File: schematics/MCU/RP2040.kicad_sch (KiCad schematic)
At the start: 28 parts, among them J2 TC2030, SW1 SW_Push, U1 W25Q128JVS, U2 XC6206PxxxMR-Regulator_Linear, U3 RP2040, Y1 12MHz

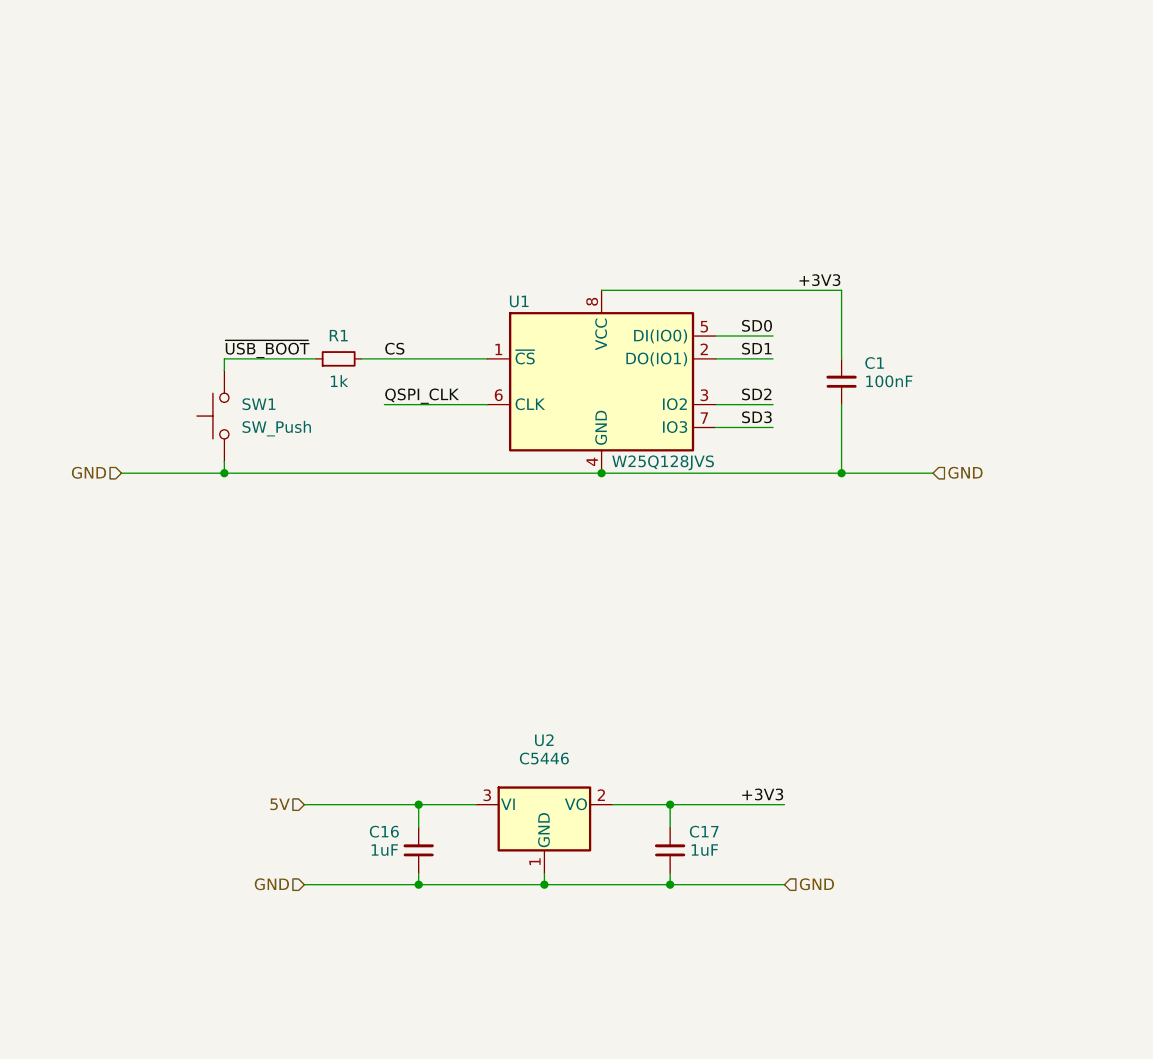
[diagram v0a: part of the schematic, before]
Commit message: restructure schematics folder
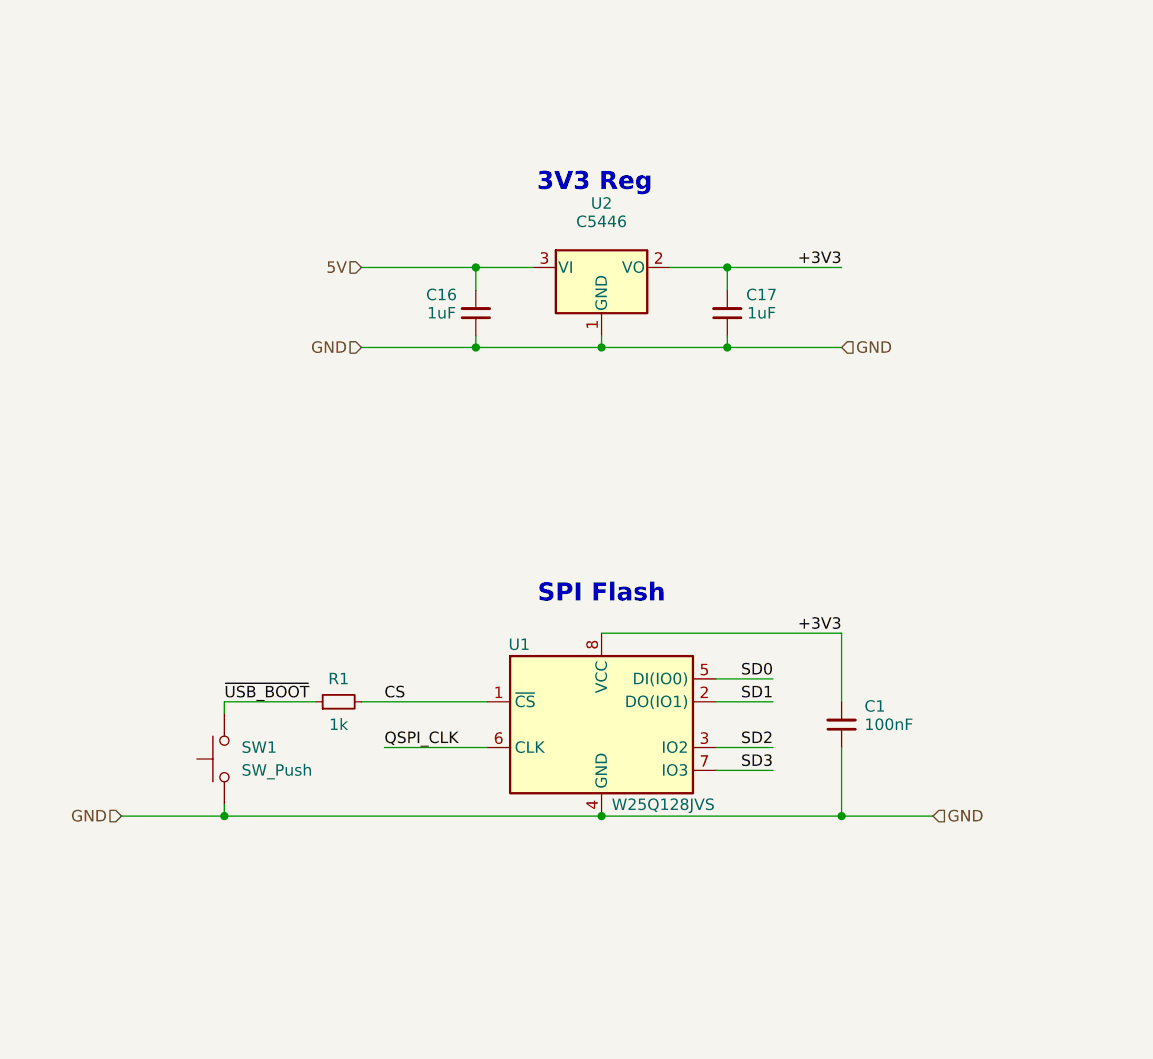
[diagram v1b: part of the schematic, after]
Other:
- note added: "3V3 Reg"
- note added: "SPI Flash"
- moved on the sheet: C1, C16, C17, R1, SW1, U1, U2

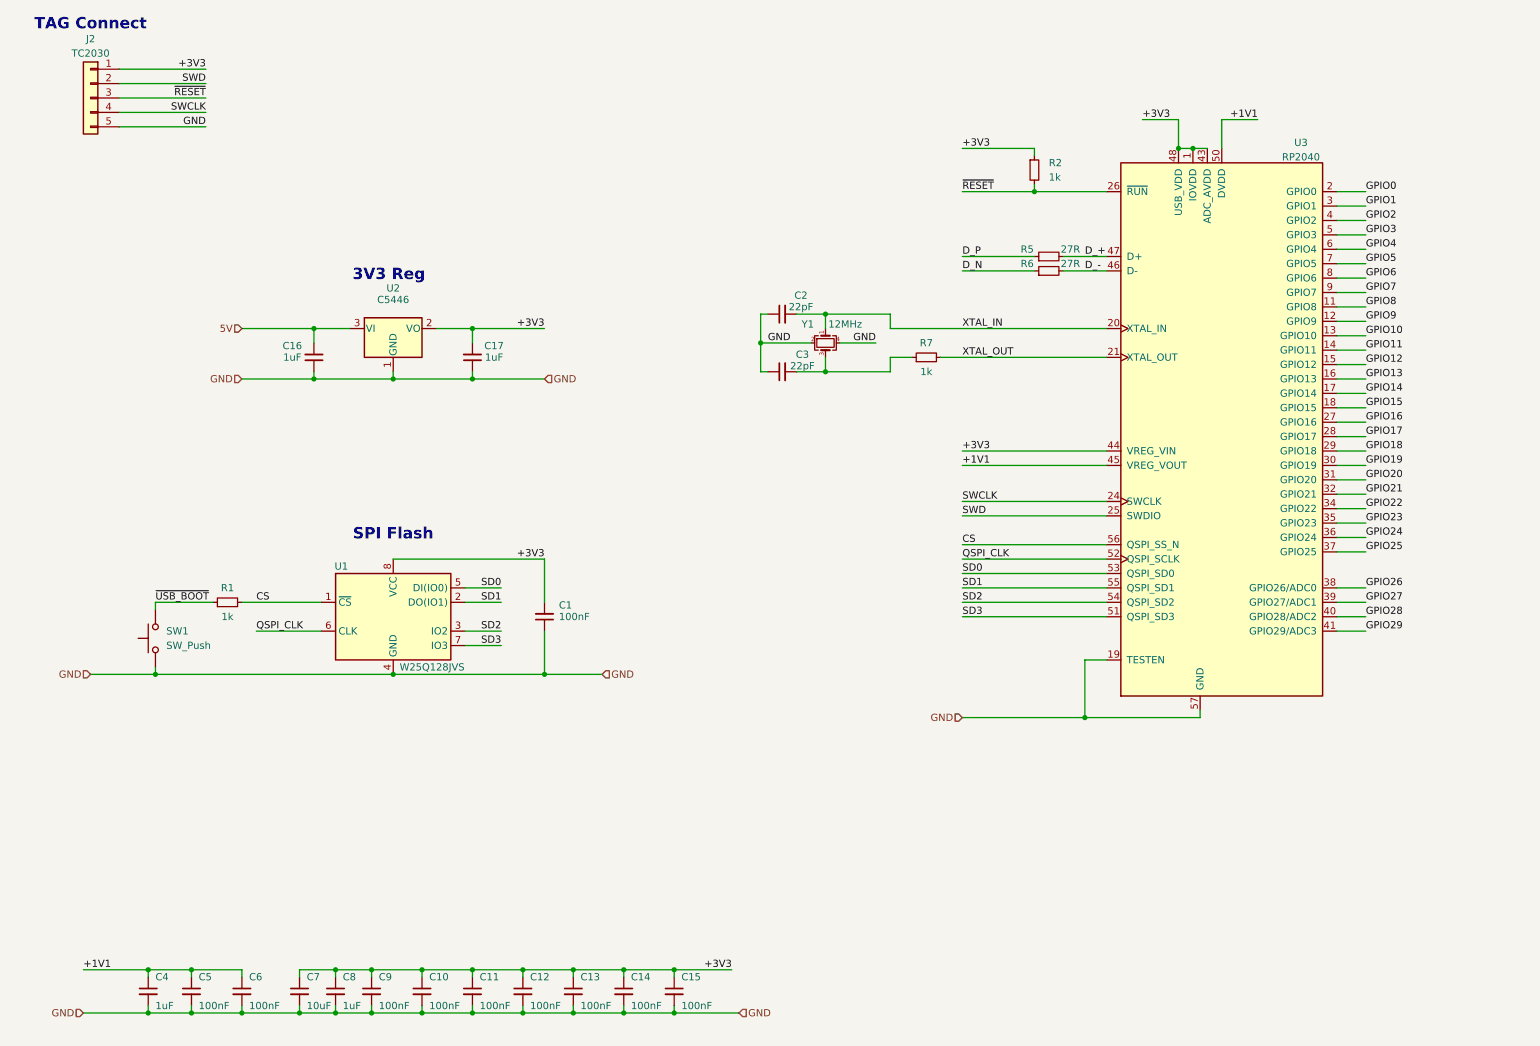
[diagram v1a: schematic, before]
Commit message: Add reset circuit to RP2040
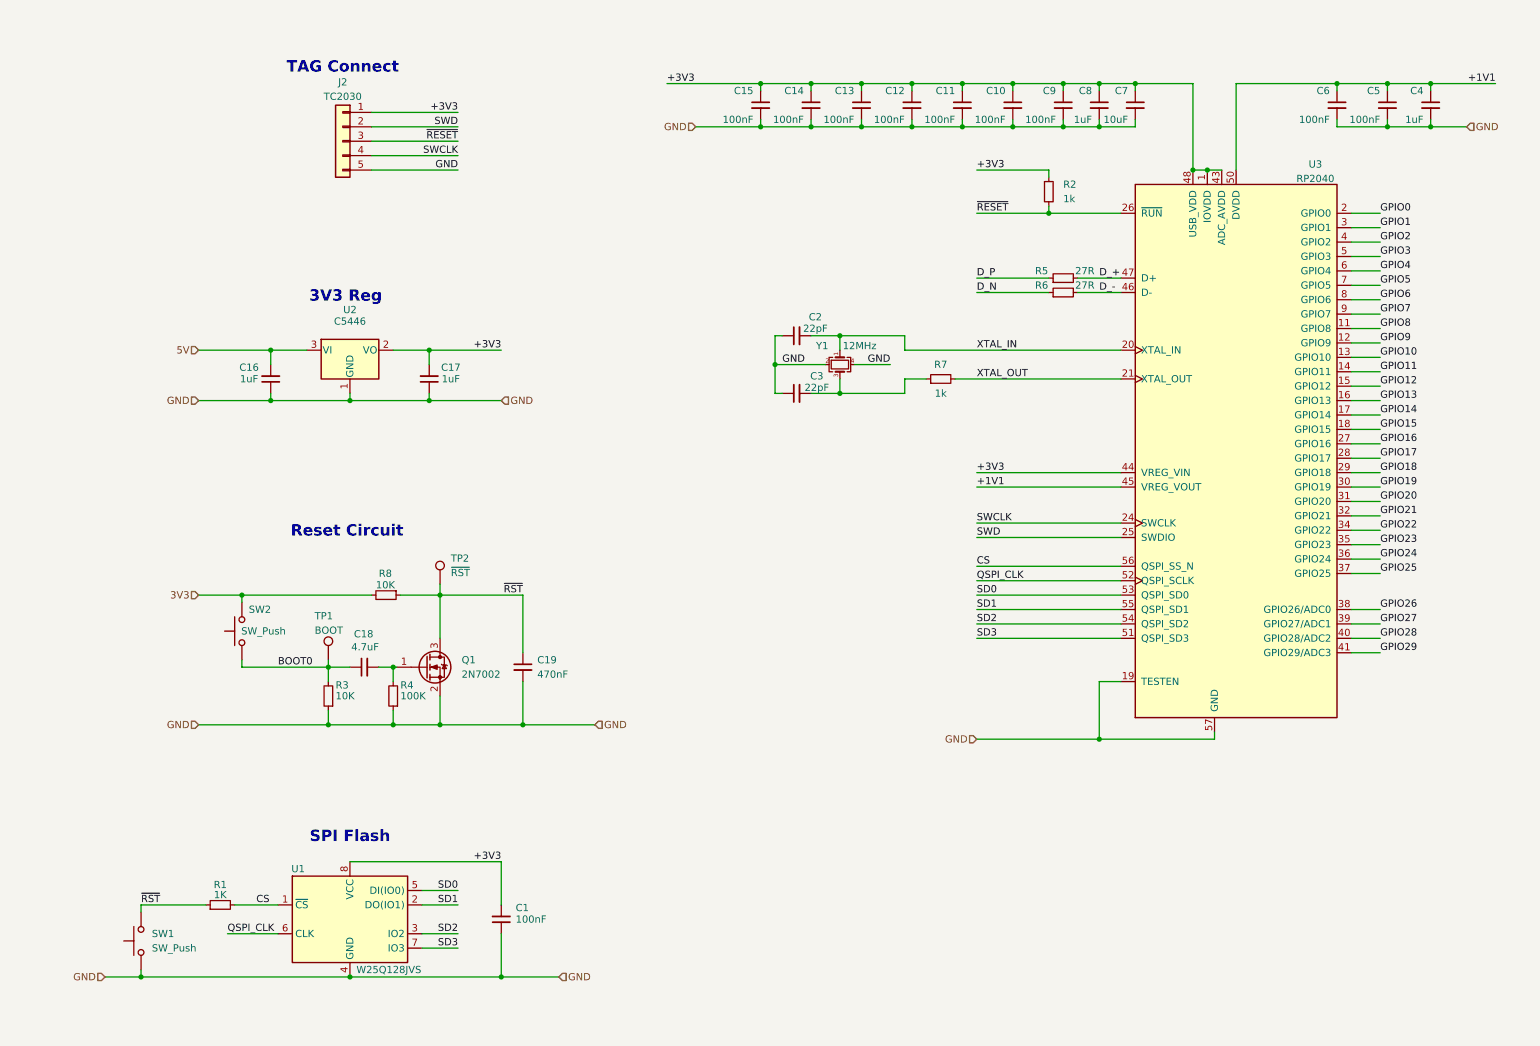
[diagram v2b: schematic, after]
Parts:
- added C18: 4.7uF, Capacitor_SMD:C_0603_1608Metric, symbol Device:C_Small
- added C19: 470nF, Capacitor_SMD:C_0603_1608Metric, symbol Device:C_Small
- added Q1: 2N7002, Package_TO_SOT_SMD:SOT-23, symbol Transistor_FET:2N7002
- added R3, R8: 10K, Resistor_SMD:R_0603_1608Metric, symbol Device:R_Small
- added R4: 100K, Resistor_SMD:R_0603_1608Metric, symbol Device:R_Small
- added SW2: SW_Push, symbol Switch:SW_Push
- added TP1: BOOT, symbol Connector:TestPoint
- added TP2: ~{RST}, symbol Connector:TestPoint
- R1: value 1k -> 1K
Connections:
- net GND: now also C19.2, Q1.2 (S), R3.1, R4.1
- net ~{USB_BOOT} renamed ~{RST}
- net ~{RST}: now also C19.1, Q1.3 (D), R8.1, TP2.1
- new net: C18.2, Q1.1 (G), R4.2
- new net 3V3: R8.2, SW2.1
- new net BOOT0: C18.1, R3.2, SW2.2, TP1.1
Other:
- note added: "Reset Circuit"
- moved on the sheet: C1, C10, C11, C12, C13, C14, C15, C16, C17, C2, C3, C4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

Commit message: Minor updates to STM32, refactor RP2040
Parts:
- removed C1: 100nF, Capacitor_SMD:C_0402_1005Metric, symbol Device:C_Small
- removed C16, C17: 1uF, Capacitor_SMD:C_0402_1005Metric, symbol Device:C_Small
- removed C18: 4.7uF, Capacitor_SMD:C_0603_1608Metric, symbol Device:C_Small
- removed C19: 470nF, Capacitor_SMD:C_0603_1608Metric, symbol Device:C_Small
- removed J2: TC2030, Connector:Tag-Connect_TC2030-IDC-NL_2x03_P1.27mm_Vertical, symbol Connector_Generic:Conn_01x05
- removed Q1: 2N7002, Package_TO_SOT_SMD:SOT-23, symbol Transistor_FET:2N7002
- removed R1: 1K, Resistor_SMD:R_0402_1005Metric, symbol Device:R_Small
- removed SW2: SW_Push, symbol Switch:SW_Push
- removed U1: W25Q128JVS, Package_SO:SOIC-8_5.23x5.23mm_P1.27mm, symbol Memory_Flash:W25Q128JVS
- added C11: 100nF, Capacitor_SMD:C_0402_1005Metric, symbol Device:C_Small
- added C6: 4.7uF, Capacitor_SMD:C_0805_2012Metric, symbol Device:C_Small
- added D20: LL4148, Diode_SMD:D_MiniMELF, symbol Diode:LL4148
- added J2: Conn_ARM_SWD_TagConnect_TC2030-NL, Connector:Tag-Connect_TC2030-IDC-NL_2x03_P1.27mm_Vertical, symbol Connector:Conn_ARM_SWD_TagConnect_TC2030-NL
- added Q1: 2N7002VC-7, Package_TO_SOT_SMD:SOT-363_SC-70-6, symbol Transistor_FET:FDG6335N
- added R5: 51K, Resistor_SMD:R_0402_1005Metric, symbol Device:R_Small
- added R6: 100K, Resistor_SMD:R_0402_1005Metric, symbol Device:R_Small
- added R7: 10K, Resistor_SMD:R_0402_1005Metric, symbol Device:R_Small
- added TP3: Boot, TestPoint:TestPoint_Pad_D1.0mm, symbol Connector:TestPoint
- added U3: GD25LQ128DYIGR, Package_SON:WSON-8-1EP_6x5mm_P1.27mm_EP3.4x4mm, symbol josh-memory:W25Q128JVSIQ
- C4, C8: value 1uF -> 10uF; LCSC C52923 -> (none); MPN (none) -> C0805C106K3PAC7800; Manufacturer (none) -> KEMET; Price (none) -> $0.43; Rating (none) -> CAP CER 10UF 25V X5R 0805; Supplier (none) -> Digikey; Supplier PN (none) -> 399-11939-1-ND
- C?: renamed from C12; LCSC C1525 -> (none); MPN (none) -> C0402C104K3RAC7867; Manufacturer (none) -> KEMET; Price (none) -> $0.33; Rating (none) -> CAP CER 0.1UF 25V X7R 0402; Supplier (none) -> Digikey; Supplier PN (none) -> 399-14148-1-ND
- C?: renamed from C7; LCSC C15525 -> (none); MPN (none) -> C0805C106K3PAC7800; Manufacturer (none) -> KEMET; Price (none) -> $0.43; Rating (none) -> CAP CER 10UF 25V X5R 0805; Supplier (none) -> Digikey; Supplier PN (none) -> 399-11939-1-ND
- C?: renamed from C15; LCSC C1525 -> (none); MPN (none) -> C0402C104K3RAC7867; Manufacturer (none) -> KEMET; Price (none) -> $0.33; Rating (none) -> CAP CER 0.1UF 25V X7R 0402; Supplier (none) -> Digikey; Supplier PN (none) -> 399-14148-1-ND
- C?: renamed from C14; LCSC C1525 -> (none); MPN (none) -> C0402C104K3RAC7867; Manufacturer (none) -> KEMET; Price (none) -> $0.33; Rating (none) -> CAP CER 0.1UF 25V X7R 0402; Supplier (none) -> Digikey; Supplier PN (none) -> 399-14148-1-ND
- C?: renamed from C11; LCSC C1525 -> (none); MPN (none) -> C0402C104K3RAC7867; Manufacturer (none) -> KEMET; Price (none) -> $0.33; Rating (none) -> CAP CER 0.1UF 25V X7R 0402; Supplier (none) -> Digikey; Supplier PN (none) -> 399-14148-1-ND
- C?: renamed from C10; LCSC C1525 -> (none); MPN (none) -> C0402C104K3RAC7867; Manufacturer (none) -> KEMET; Price (none) -> $0.33; Rating (none) -> CAP CER 0.1UF 25V X7R 0402; Supplier (none) -> Digikey; Supplier PN (none) -> 399-14148-1-ND
- C?: renamed from C2; LCSC C1555 -> (none); MPN (none) -> C0402C220J4GAC7867; Manufacturer (none) -> KEMET; Price (none) -> 0.16; Rating (none) -> CAP CER 22PF 16V C0G/NP0 0402; Supplier (none) -> Digikey; Supplier PN (none) -> 399-C0402C220J4GAC7867CT-ND
- C?: renamed from C13; LCSC C1525 -> (none); MPN (none) -> C0402C104K3RAC7867; Manufacturer (none) -> KEMET; Price (none) -> $0.33; Rating (none) -> CAP CER 0.1UF 25V X7R 0402; Supplier (none) -> Digikey; Supplier PN (none) -> 399-14148-1-ND
- C?: renamed from C5; LCSC C1525 -> (none); MPN (none) -> C0402C104K3RAC7867; Manufacturer (none) -> KEMET; Price (none) -> $0.33; Rating (none) -> CAP CER 0.1UF 25V X7R 0402; Supplier (none) -> Digikey; Supplier PN (none) -> 399-14148-1-ND
- C?: renamed from C3; LCSC C1555 -> (none); MPN (none) -> C0402C220J4GAC7867; Manufacturer (none) -> KEMET; Price (none) -> 0.16; Rating (none) -> CAP CER 22PF 16V C0G/NP0 0402; Supplier (none) -> Digikey; Supplier PN (none) -> 399-C0402C220J4GAC7867CT-ND
- C?: renamed from C9; LCSC C1525 -> (none); MPN (none) -> C0402C104K3RAC7867; Manufacturer (none) -> KEMET; Price (none) -> $0.33; Rating (none) -> CAP CER 0.1UF 25V X7R 0402; Supplier (none) -> Digikey; Supplier PN (none) -> 399-14148-1-ND
- C?: renamed from C6; LCSC C1525 -> (none); MPN (none) -> C0402C104K3RAC7867; Manufacturer (none) -> KEMET; Price (none) -> $0.33; Rating (none) -> CAP CER 0.1UF 25V X7R 0402; Supplier (none) -> Digikey; Supplier PN (none) -> 399-14148-1-ND
- R3: footprint Resistor_SMD:R_0603_1608Metric -> Resistor_SMD:R_0402_1005Metric; MPN (none) -> RC0402FR-0710KL; Manufacturer (none) -> YAGEO; Price (none) -> $0.16; Rating (none) -> RES 10K OHM 1% 1/16W 0402; Supplier (none) -> Digikey; Supplier PN (none) -> 311-10.0KLRCT-ND
- R4: value 100K -> 10K; footprint Resistor_SMD:R_0603_1608Metric -> Resistor_SMD:R_0402_1005Metric; MPN (none) -> RC0402FR-0710KL; Manufacturer (none) -> YAGEO; Price (none) -> $0.16; Rating (none) -> RES 10K OHM 1% 1/16W 0402; Supplier (none) -> Digikey; Supplier PN (none) -> 311-10.0KLRCT-ND
- R8: value 10K -> 1K; footprint Resistor_SMD:R_0603_1608Metric -> Resistor_SMD:R_0402_1005Metric; MPN (none) -> RC0402FR-071KL; Manufacturer (none) -> YAGEO; Price (none) -> $0.16; Rating (none) -> RES 1K OHM 1% 1/16W 0402; Supplier (none) -> Digikey; Supplier PN (none) -> 311-1.00KLRCT-ND
- R?: renamed from R2; value 1k -> 1K; LCSC C11702 -> (none); MPN (none) -> RC0402FR-071KL; Manufacturer (none) -> YAGEO; Price (none) -> $0.16; Rating (none) -> RES 1K OHM 1% 1/16W 0402; Supplier (none) -> Digikey; Supplier PN (none) -> 311-1.00KLRCT-ND
- R?: renamed from R5; footprint Resistor_SMD:R_0603_1608Metric -> Resistor_SMD:R_0402_1005Metric; LCSC C25190 -> (none); MPN (none) -> RC0402FR-0727RL; Manufacturer (none) -> YAGEO; Price (none) -> $0.16; Rating (none) -> RES 27 Ohms ±1% 0.063W, 1/16W Chip Resistor 0402 (1005 Metr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; Supplier (none) -> Digikey; Supplier PN (none) -> YAG3086CT-ND
- R?: renamed from R6; footprint Resistor_SMD:R_0603_1608Metric -> Resistor_SMD:R_0402_1005Metric; LCSC C25190 -> (none); MPN (none) -> RC0402FR-0727RL; Manufacturer (none) -> YAGEO; Price (none) -> $0.16; Rating (none) -> RES 27 Ohms ±1% 0.063W, 1/16W Chip Resistor 0402 (1005 Metr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; Supplier (none) -> Digikey; Supplier PN (none) -> YAG3086CT-ND
- R?: renamed from R7; value 1k -> 1K; LCSC C11702 -> (none); MPN (none) -> RC0402FR-071KL; Manufacturer (none) -> YAGEO; Price (none) -> $0.16; Rating (none) -> RES 1K OHM 1% 1/16W 0402; Supplier (none) -> Digikey; Supplier PN (none) -> 311-1.00KLRCT-ND
- SW1: value SW_Push -> SWITCH; footprint Connector_PinSocket_2.54mm:PinSocket_1x02_P2.54mm_Vertical -> (none); now in the parts list
- TP1: value BOOT -> Reset; footprint (none) -> TestPoint:TestPoint_Pad_D1.0mm
- TP2: value ~{RST} -> Delay; footprint (none) -> TestPoint:TestPoint_Pad_D1.0mm
- U?: renamed from U3; footprint Sleep-Lib:RP2040-QFN-56 -> Package_DFN_QFN:QFN-56-1EP_7x7mm_P0.4mm_EP3.2x3.2mm; LCSC C2040 -> (none); MPN (none) -> SC0914(13); Manufacturer (none) -> Raspberry Pi; Price (none) -> $1.11; Rating (none) -> IC MCU 32BIT EXT MEM 56QFN; Supplier (none) -> Digikey; Supplier PN (none) -> 2648-SC0914(13)CT-ND
- U?: renamed from U2; LCSC C5446 -> (none)
- Y?: renamed from Y1; footprint Crystal:Crystal_SMD_3225-4Pin_3.2x2.5mm -> Crystal_SMD_Abracon_ABM8G-4Pin_3.2x2.5mm; LCSC C9002 -> (none); MPN (none) -> ABM8-12.000MHZ-12-B1U-T; Manufacturer (none) -> Abracon LLC; Price (none) -> $0.67; Rating (none) -> CRYSTAL 12.0000MHZ 12PF SMD; Supplier (none) -> Digikey; Supplier PN (none) -> 535-14962-1-ND
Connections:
- net CS is gone; now on net QSPI_nCS: U?.56 (QSPI_SS_N)
- net ~{RESET} is gone; now on net ~{RST}: R?.2, U?.26 (~{RUN})
- net 5V: now also C4.1
- net DVDD: no longer C4.1
- net GND: now also C11.2, C6.2, J2.5 (GND), Q1.1 (S), Q1.3 (D), R6.1, U3.4 (GND), U3.9 (GND); no longer R3.1, SW1.1
- net IOVDD: now also R3.2, SW1.2, C11.1, J2.1 (VCC), R7.2, U3.8 (VCC); no longer C8.1
- net SWCLK: now also J2.4 (SWCLK)
- net ~{RST}: now also R3.1, TP1.1, J2.3 (~{RESET}), Q1.6 (D); no longer R8.1, SW1.2, TP2.1
- net at R4.2: now also SW1.1, D20.2 (A), Q1.2 (G)
- net 3V3 renamed QSPI_nCS
- net QSPI_nCS: now also R7.1, U3.1 (~{CS})
- removed net BOOT0: R3.2, TP1.1
- net D_+: no longer names the net of R?.2, U?.47 (D+)
- net D_-: no longer names the net of R?.2, U?.46 (D-)
- net QSPI_CLK renamed QSPI_SCLK
- net QSPI_SCLK: now also U3.6 (CLK)
- net SD0 renamed QSPI_SD0
- net QSPI_SD0: now also U3.5 (DI(IO0))
- net SD1 renamed QSPI_SD1
- net QSPI_SD1: now also U3.2 (DO(IO1))
- net SD2 renamed QSPI_SD2
- net QSPI_SD2: now also U3.3 (IO2)
- net SD3 renamed QSPI_SD3
- net QSPI_SD3: now also U3.7 (IO3)
- net SWD renamed SWDIO
- net SWDIO: now also J2.2 (SWDIO)
- net XTAL_IN: no longer names the net of C?.2, U?.20 (XTAL_IN), Y?.1
- net XTAL_OUT: no longer names the net of R?.2, U?.21 (XTAL_OUT)
- new net: Q1.4 (S), R8.1, TP3.1
- new net: C6.1, C8.1, Q1.5 (G), R5.1, R6.2, TP2.1
- new net: D20.1 (K), R5.2
- no-connect marks 0 -> 1
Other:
- note added: "Q1B - using body diode due to lack of space. Can sub with normal diode"
- note added: "Q2A - pulls nRST to GND"
- note added: "Q2B - pulls nCS to GND"
- note added: "RC delay"
- note added: "Reset / Boot Circuit"
- note added: "Tap for < 500ms to reset Hold for > 500ms to enter UF2 bootloader"
- note removed: "Reset Circuit"
- moved on the sheet: C?, R?, U?, Y?

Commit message: Fix library footprint link
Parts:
- Y?: footprint Crystal_SMD_Abracon_ABM8G-4Pin_3.2x2.5mm -> Crystal:Crystal_SMD_Abracon_ABM8G-4Pin_3.2x2.5mm
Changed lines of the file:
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@@
 			)
 		)
-		(property "Footprint" "Crystal_SMD_Abracon_ABM8G-4Pin_3.2x2.5mm"
+		(property "Footprint" "Crystal:Crystal_SMD_Abracon_ABM8G-4Pin_3.2x2.5mm"
 			(at 194.31 88.9 0)
 			(effects
